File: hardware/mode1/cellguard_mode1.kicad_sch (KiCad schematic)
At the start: 19 parts, among them J1 Raspberry Pi 5 GPIO Header, J2 ZY12PDN PD Trigger (5V), J3 ATORCH BW150 부하 입력, K1 4CH Relay [SZH-RLBG-012], U1 INA226 [VLT-VCM029], U2 Battery Babysitter [PRT-13777], U3 MLX90614 [SEN0206], U4 ADS1115 [VLT-AD004], U5 DS18B20 방수형 [SEN050007], U6 OLED 0.96in SPI [CN0219]

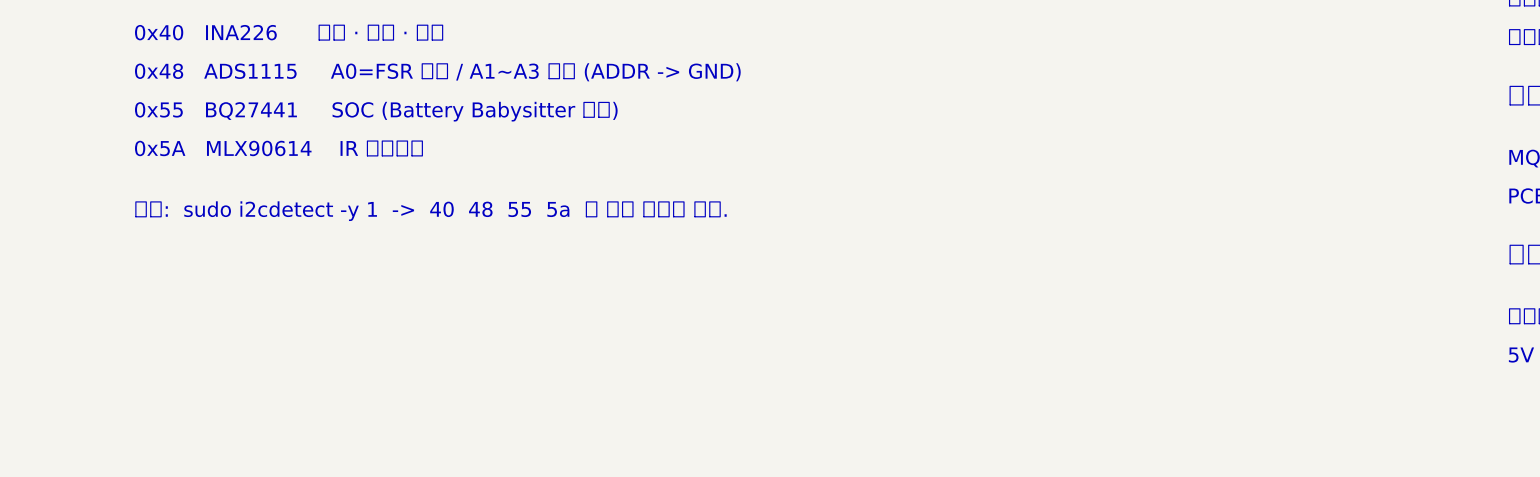
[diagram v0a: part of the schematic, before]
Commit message: fix(hw): MLX90614 갱신주기 정정(500ms -> 864.9ms)과 피크값 정책 확립
갱신주기 재확인 결과 이전에 적은 "약 500ms"가 틀렸다. Melexis 앱노트의
정착시간 공식 Tset = 9.719 + IIR x (FIR+5.26) + IIR x (FIR+12.542) 에
공장 기본값(IIR 50% -> IIRSetting 10, FIR 1024 -> FIRSetting 33.856)을
넣으면 864.859ms 로, 앱노트가 명시한 기본값과 정확히 일치한다. 즉
MLX90614는 DS18B20(750ms)보다도 느린, BQ27441 다음으로 느린 센서였다.

피크값 사용 요청에 대해 두 가지를 분리했다.

- 공간 피크(FOV 안 최고온점)는 불가능하다. MLX90614는 서모파일 소자
  1개짜리라 데이터시트가 "measured value is the average temperature of
  all objects in the Field Of View" 라고 명시한다. 설정이 아니라 물리다.
  대신 SEN0206(= MLX90614-DCC, FOV 35도)의 스팟 지름이 0.63 x 거리 이므로
  셀에서 2cm 이내에 부착하면 1.26cm 로 18650 지름 안에 들어가 배경이
  섞이지 않는다. 5cm 면 3.15cm 라 배경이 절반 넘게 섞인다.

- 시간축 피크(100ms 창의 최댓값)는 가능하되 EEPROM 재설정이 선행돼야
  한다. 공장 기본 IIR 50% 는 "최대 스텝 0.5" 라 입력이 튀어도 출력이
  절반까지만 따라간다 - 열폭주 초기 스파이크가 바로 그 신호인데 기본
  설정이 이를 깎아낸다. IIR=100(감쇠 없음) + FIR=111 로 바꾸면 95.2ms 가
  되어 100ms 프레임에 실측으로 들어온다. FIR=110 이면 62.5ms(창당 2샘플,
  노이즈 약 1.23배).

ConfigRegister1(EEPROM 0x05, SMBus 커맨드 0x25)의 비트 3은 건드리면
공장 캘리브레이션이 취소되므로 read-modify-write 를 강제했다.

Co-Authored-By: Claude Opus 5 <noreply@anthropic.com>
Claude-Session: https://claude.ai/code/session_01P42KJDHQDoWwm91ffeSx77
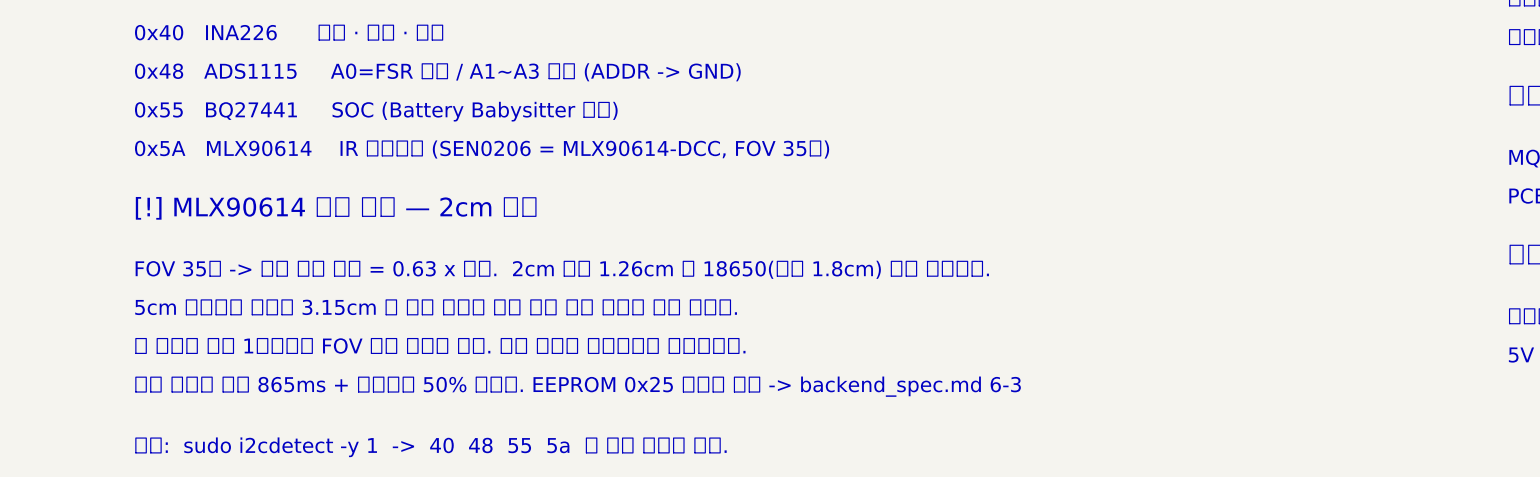
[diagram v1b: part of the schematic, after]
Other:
- note added: "0x5A MLX90614 IR 표면온도 (SEN0206 = MLX90614-DCC, FOV 35도)"
- note added: "5cm 떨어지면 스팟이 3.15cm 라 배경 온도가 절반 넘게 섞여 셀보다 낮게 읽힌다."
- note added: "FOV 35도 -> 측정 스팟 지름 = 0.63 x 거리. 2cm 에서 1.26cm 로 18650(지름 1.8cm) 안에 들어간다."
- note added: "[!] MLX90614 부착 거리 — 2cm 이내"
- note added: "이 센서는 소자 1개짜리라 FOV 안의 평균만 낸다. 공간 피크는 물리적으로 불가능하다."
- note added: "출고 상태는 갱신 865ms + 스파이크 50% 감쇠다. EEPROM 0x25 재설정 필수 -> backend_spec.md 6-3"
- note removed: "0x5A MLX90614 IR 표면온도"
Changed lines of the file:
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@@
 		(effects (font (face "Apple SD Gothic Neo") (size 2.0 2.0)) (justify left bottom))
 	)
-	(text "0x5A   MLX90614    IR 표면온도"
+	(text "0x5A   MLX90614    IR 표면온도 (SEN0206 = MLX90614-DCC, FOV 35도)"
 		(exclude_from_sim no)
 		(at 215.00 369.20 0)
 		(effects (font (face "Apple SD Gothic Neo") (size 2.0 2.0)) (justify left bottom))
 	)
+	(text "[!] MLX90614 부착 거리 — 2cm 이내"
+		(exclude_from_sim no)
+		(at 215.00 377.40 0)
+		(effects (font (face "Apple SD Gothic Neo") (size 2.5 2.5)) (justify left bottom))
+	)
+	(text "FOV 35도 -> 측정 스팟 지름 = 0.63 x 거리.  2cm 에서 1.26cm 로 18650(지름 1.8cm) 안에 들어간다."
+		(exclude_from_sim no)
+		(at 215.00 385.40 0)
+		(effects (font (face "Apple SD Gothic Neo") (size 2.0 2.0)) (justify left bottom))
+	)
+	(text "5cm 떨어지면 스팟이 3.15cm 라 배경 온도가 절반 넘게 섞여 셀보다 낮게 읽힌다."
+		(exclude_from_sim no)
+		(at 215.00 390.60 0)
+		(effects (font (face "Apple SD Gothic Neo") (size 2.0 2.0)) (justify left bottom))
+	)
+	(text "이 센서는 소자 1개짜리라 FOV 안의 평균만 낸다. 공간 피크는 물리적으로 불가능하다."
+		(exclude_from_sim no)
+		(at 215.00 395.80 0)
+		(effects (font (face "Apple SD Gothic Neo") (size 2.0 2.0)) (justify left bottom))
+	)
+	(text "출고 상태는 갱신 865ms + 스파이크 50% 감쇠다. EEPROM 0x25 재설정 필수 -> backend_spec.md 6-3"
+		(exclude_from_sim no)
+		(at 215.00 401.00 0)
+		(effects (font (face "Apple SD Gothic Neo") (size 2.0 2.0)) (justify left bottom))
+	)
 	(text "확인:  sudo i2cdetect -y 1  ->  40  48  55  5a  네 개가 보여야 한다."
 		(exclude_from_sim no)
-		(at 215.00 377.40 0)
+		(at 215.00 409.20 0)
 		(effects (font (face "Apple SD Gothic Neo") (size 2.0 2.0)) (justify left bottom))
 	)

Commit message: feat(hw): 온도를 다점 측정으로 확장해 공간 피크 구현
MLX90614 소자 1개는 데이터시트대로 FOV 안 모든 물체의 '평균'만 낸다.
열폭주는 국부에서 시작하므로 센서 1개로는 한 귀퉁이의 과열이 희석돼
사라진다. 억지로라도 공간 피크를 만들 방법을 찾다가 프로젝트 문서의
제약 하나가 사실이 아님을 확인했다.

MLX90614는 I2C 주소가 고정이 아니다. 데이터시트 EEPROM 맵에
"SMBus address (LSB only) | 0x0E | Write access: Yes" 로 명시돼 있고
Figure 36 이 "Use of multiple MLX90614 devices in SMBus network" 다.
한 버스에 127개까지 붙는다. 고정인 건 BQ27441(0x55) 뿐이므로
CLAUDE.md / PLAN.md / AGENTS.md 의 "둘 다 주소 고정" 서술을 정정했다.

그래서 예비품으로 잡아 뒀던 센서를 전부 투입해 다점화했다.

- DS18B20 x3 -> 셀 하단 / 중앙 / 단자쪽. 같은 GPIO4 버스에 병렬.
  1-Wire 는 고유 64비트 ROM 코드를 쓰므로 주소 설정이 필요 없고,
  Skip ROM + Convert T 로 동시 변환하면 개수가 늘어도 750ms 그대로다.
- MLX90614 x2 -> 셀 중앙(0x5A) / 단자쪽(0x5B). 양극 단자 부근이
  내부저항 + 접촉저항 때문에 가장 먼저 뜨거워지는 지점이다.
- temp_contact / temp_ir_surface 는 각 그룹의 최댓값. IR 은 시간축
  피크(창 안 최댓값) 위에 공간축 피크(두 존 중 큰 쪽)를 얹는다.
- temp_points 로 개별 지점값을 함께 발행한다(길이 고정 3/2, 위치 순서,
  결측은 null). 지점 간 온도차 자체가 국부 과열의 직접 증거다.
  기존 스칼라 필드는 그대로라 AI/대시보드 소비자는 고칠 게 없다.

시트가 A2 로는 주석을 못 담아 A1 으로 키우고 열 간격을 넓혔다.

검증: ERC 위반 0건. 네트리스트로 OW_DATA 5노드(U5/U7/U8 포함),
I2C_SDA/SCL 각 6노드(U9 포함), CELL_N 이 GND 와 분리된 것 재확인.

Co-Authored-By: Claude Opus 5 <noreply@anthropic.com>
Claude-Session: https://claude.ai/code/session_01P42KJDHQDoWwm91ffeSx77
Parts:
- added U7: DS18B20 #2 (셀 중앙), symbol cellguard:DS18B20
- added U8: DS18B20 #3 (셀 상단·단자쪽), symbol cellguard:DS18B20
- added U9: MLX90614 #2 (0x5B, 셀 단자쪽), symbol cellguard:MLX90614
- U3: value MLX90614 [SEN0206] -> MLX90614 #1 (0x5A, 셀 중앙)
- U5: value DS18B20 방수형 [SEN050007] -> DS18B20 #1 (셀 하단)
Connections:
- net +3V3: now also U7.1 (VDD), U8.1 (VDD), U9.1 (VCC)
- net GND: now also U7.3 (GND), U8.3 (GND), U9.2 (GND)
- net I2C_SCL: now also U9.4 (SCL)
- net I2C_SDA: now also U9.3 (SDA)
- net OW_DATA: now also U7.2 (DQ), U8.2 (DQ)
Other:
- note added: "0x5A MLX90614 #1 IR 표면온도 - 셀 중앙 (SEN0206 = MLX90614-DCC, FOV 35도)"
- note added: "0x5B MLX90614 #2 IR 표면온도 - 셀 단자쪽 (EEPROM 0x0E 로 주소 변경한 개체)"
- note added: "5V 3A+ 어댑터, 캡톤 테이프 · 서멀 패드 x3, 외장 케이스."
- note added: "DS18B20 3개는 같은 3선(GPIO4 + 3.3V + GND)에 병렬로 문다. 1-Wire는 고유 64비트 ROM 코드를"
- note added: "MLX90614 소자 1개는 FOV 안의 '평균'만 낸다. 그래서 2개를 다른 지점에 겨눠 공간 피크를 만든다."
- note added: "[!] 온도는 다점 측정 -> 최댓값을 쓴다"
- note added: "temp_ir_surface = max(#1, #2) temp_contact = max(DS18B20 #1, #2, #3)"
- note added: "물리핀 7 GPIO4 1-Wire (+ 4.7k 풀업 -> 3.3V) -> DS18B20 x3 (병렬)"
- note added: "쓰므로 주소 설정이 필요 없다. Skip ROM + Convert T 로 셋을 동시에 변환해 750ms 그대로다."
- note added: "예비품 없음: DS18B20 3개와 MLX90614 2개를 전부 투입했다. 고장 시 교체품이 없다."
- note removed: "0x5A MLX90614 IR 표면온도 (SEN0206 = MLX90614-DCC, FOV 35도)"
- note removed: "5V 3A+ 어댑터, 캡톤 테이프 · 서멀 패드, 외장 케이스."
- note removed: "물리핀 7 GPIO4 1-Wire (+ 4.7k 풀업 -> 3.3V) -> DS18B20"
- note removed: "이 센서는 소자 1개짜리라 FOV 안의 평균만 낸다. 공간 피크는 물리적으로 불가능하다."
- moved on the sheet: J1, J2, J3, K1, R2, R3, R4, R5, R6, U2, U3, U4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

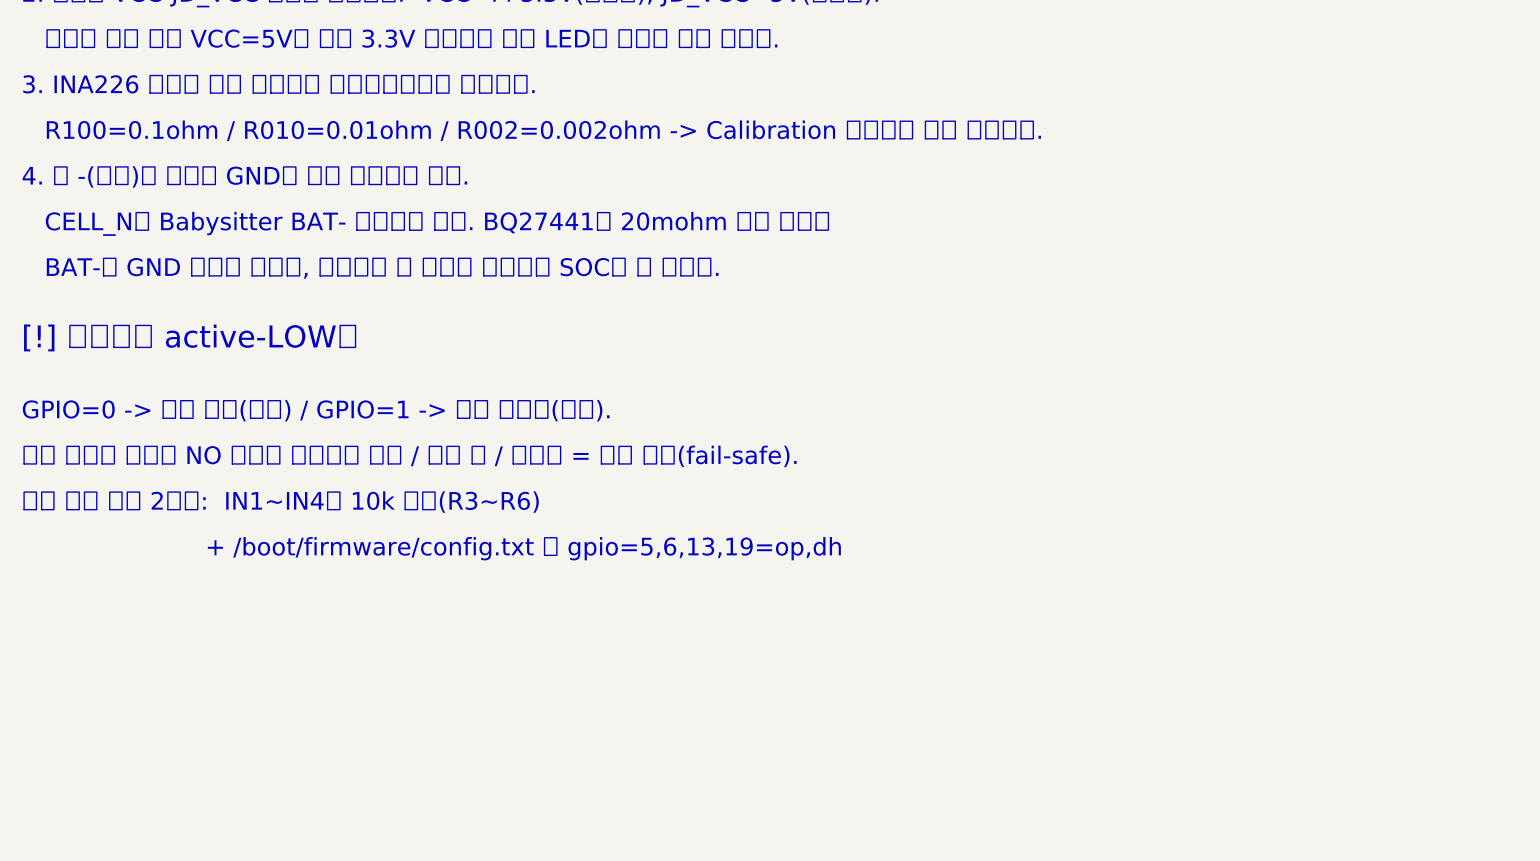
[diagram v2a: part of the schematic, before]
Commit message: fix(hw): 백엔드 스펙 검증 — 치명적 사실오류 3건 정정, §1 재작성
Sonnet 5 서브에이전트 2대로 데이터시트 대조 검증과 문서 정합성 감사를
돌리고, 치명적 지적은 원문으로 직접 재확인한 뒤 반영했다.

## 치명적 사실오류 (구현했다면 조용히 틀렸을 것들)

1. BQ27441 Flags(0x06) 비트 3개가 틀렸다. TRM Table 4-4 가 High/Low
   바이트를 각각 bit7..bit0 으로 표기하는데 이를 절대 비트로 잘못
   환산했다. ITPOR 은 bit 8 이 아니라 bit 5 이고, bit 8 은 CHG(충전
   허용)다. 옛 표대로 구현하면 충전할 때마다 "게이지 리셋됨"으로
   오탐하고 정작 진짜 리셋(ITPOR)은 영영 못 잡는다. OT 는 bit 15,
   FC 는 bit 9 로 서로 뒤바뀌어 있었다.

2. BQ27441 AveragePower 주소가 0x16 이 아니라 0x18 이다. 0x16/0x17 은
   표준 커맨드에 존재하지 않는 주소다. (TRM Table 4-1)

3. INA226 "최대 측정 전류 20A/8A/0.8A" 가 틀렸다. 상한을 정하는 건
   션트가 아니라 16비트 Current 레지스터다. Current_LSB=0.0001A 면
   션트값과 무관하게 32767 x 0.0001 = 3.28A 에서 넘치고, 넘치면 부호가
   뒤집혀 방전이 충전으로 보인다. 실제 상한은 3.28/3.28/0.82A.
   TI 가 이 실패모드용으로 Mask/Enable(0x06) bit 2 에 OVF 플래그를
   두었으므로 매 프레임 확인하도록 오류 처리에 추가했다.

## §1 재작성

MLX90614 가 500ms 이고 센서가 각 1개이던 시절 문장이 남아 있었다.
- "새 값이 나오는 센서는 INA226 하나뿐" -> 표에 ADS1115 가 7.8ms 로
  적혀 있어 자기모순이었다. INA226 + ADS1115 로 정정.
- "온도는 7~8개가 복사본" -> 두 온도 필드의 주기가 이제 완전히 다르다.
  IR 은 재설정 후 매 프레임 실측, 접촉은 750ms 고정으로 분리 서술.
- "가장 느린 센서(750ms)" -> BQ27441 1000ms, bulk read 미지원 시
  DS18B20 2250ms 로 정정.
- 신선도 예시 JSON 에 temp_points 추가. MLX 2개는 순차 읽기라 지점
  간 age 가 어긋날 수 있음을 명시.
- 9비트 옵션이 3개 동시 변환에도 그대로 적용됨을 명시.

## 그 밖

- MLX90614 노이즈 관계 인용의 출처를 앱노트 -> 데이터시트로 정정.
  원문은 정착시간이 아니라 탭 수 기준이라 1024->512 는 1.23배가 아니라
  약 1.41배(√2)다.
- Pi 5 에서 config.txt 의 gpio= 지시문이 동작하는지는 확인이 필요하다.
  공식 문서는 여전히 문서화하고 Pi 5 제외 문구도 없으므로 "동작 안 함"
  으로 단정하지 않고, 3겹 방어 중 하드웨어 풀업만이 소프트웨어에
  의존하지 않는 층임을 명시하고 확인법(pinctrl get)을 넣었다.
- §6 헤더를 MLX90614 x2 (0x5A/0x5B) 로 복수화.
- PLAN.md 줄번호 인용 8건이 전부 깨져 있어 절 이름 인용으로 바꿨다.
  줄번호는 문서가 편집될 때마다 다시 깨진다.
- §14 "실물로 확인해야 하는 것" 신설 (H1~H7).

검증: ERC 위반 0건. 문서 내 §참조 전수 검사 결과 깨진 참조 0건.

Co-Authored-By: Claude Opus 5 <noreply@anthropic.com>
Claude-Session: https://claude.ai/code/session_01P42KJDHQDoWwm91ffeSx77
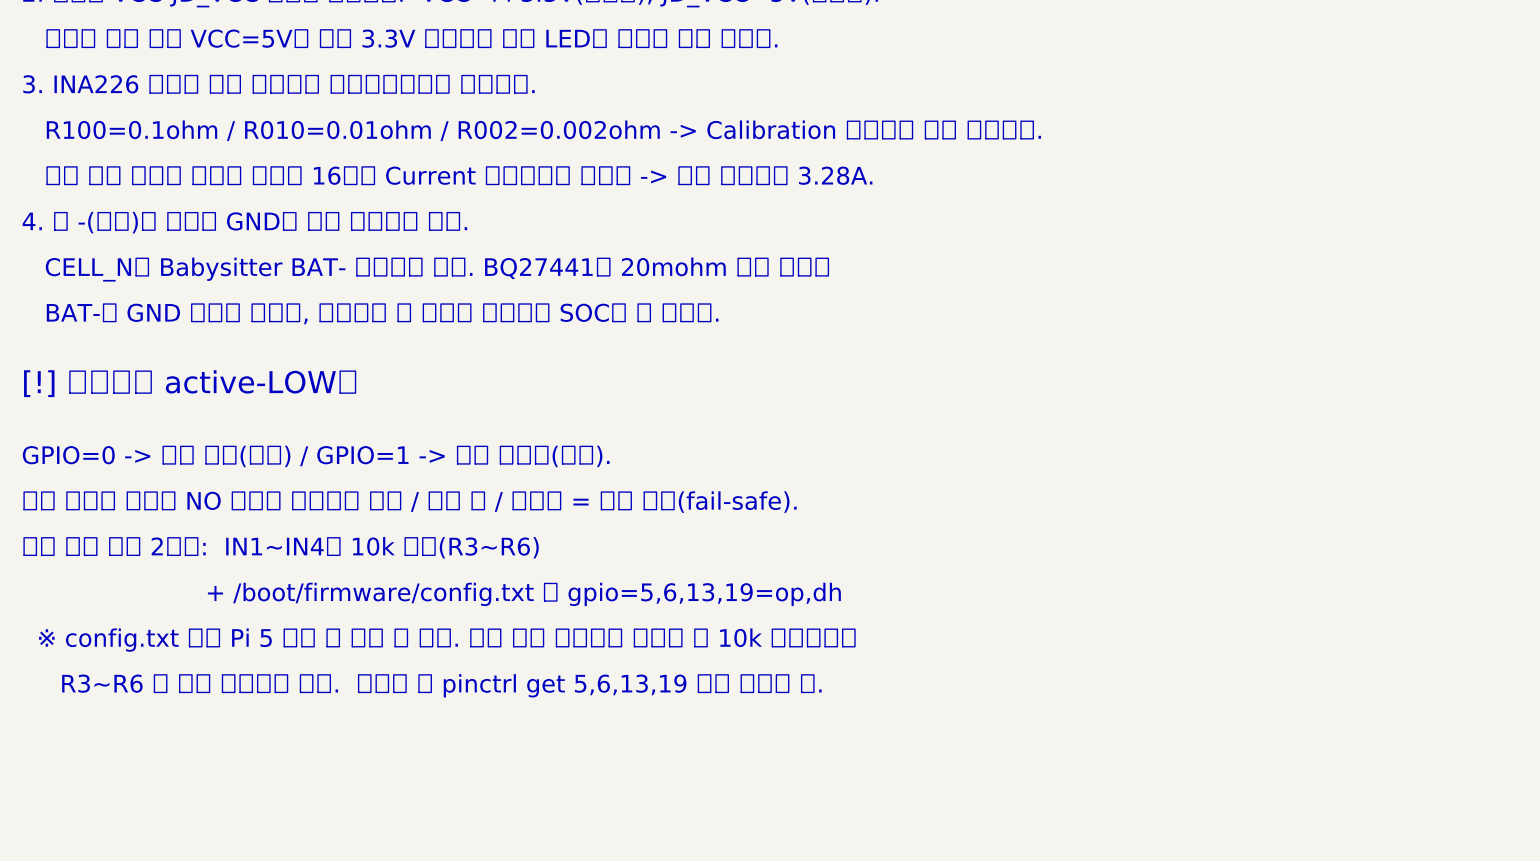
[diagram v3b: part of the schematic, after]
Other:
- note added: "R3~R6 을 절대 생략하지 마라. 재부팅 후 pinctrl get 5,6,13,19 으로 확인할 것."
- note added: "※ config.txt 쪽은 Pi 5 에서 안 먹을 수 있다. 전원 인가 순간부터 확실한 건 10k 풀업뿐이니"
- note added: "전류 측정 상한은 션트가 아니라 16비트 Current 레지스터가 정한다 -> 기본 설정에서 3.28A."
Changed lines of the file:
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@@
+		(effects (font (face "Apple SD Gothic Neo") (size 2.0 2.0)) (justify left bottom))
+	)
+	(text "   전류 측정 상한은 션트가 아니라 16비트 Current 레지스터가 정한다 -> 기본 설정에서 3.28A."
+		(exclude_from_sim no)
+		(at 20.00 371.80 0)
 		(effects (font (face "Apple SD Gothic Neo") (size 2.0 2.0)) (justify left bottom))
 	)
 	(text "4. 셀 -(음극)를 시스템 GND에 직접 연결하지 마라."
 		(exclude_from_sim no)
-		(at 20.00 371.80 0)
+		(at 20.00 377.00 0)
 		(effects (font (face "Apple SD Gothic Neo") (size 2.0 2.0)) (justify left bottom))
 	)
 	(text "   CELL_N은 Babysitter BAT- 하나에만 간다. BQ27441의 20mohm 센스 저항이"
 		(exclude_from_sim no)
-		(at 20.00 377.00 0)
+		(at 20.00 382.20 0)
 		(effects (font (face "Apple SD Gothic Neo") (size 2.0 2.0)) (justify left bottom))
 	)
 	(text "   BAT-와 GND 사이에 있어서, 직결하면 이 저항이 단락되고 SOC가 안 나온다."
 		(exclude_from_sim no)
-		(at 20.00 382.20 0)
+		(at 20.00 387.40 0)
 		(effects (font (face "Apple SD Gothic Neo") (size 2.0 2.0)) (justify left bottom))
 	)
 	(text "[!] 릴레이는 active-LOW다"
 		(exclude_from_sim no)
-		(at 20.00 390.40 0)
+		(at 20.00 395.60 0)
 		(effects (font (face "Apple SD Gothic Neo") (size 2.5 2.5)) (justify left bottom))
 	)
 	(text "GPIO=0 -> 접점 붙음(도통) / GPIO=1 -> 접점 떨어짐(차단)."
 		(exclude_from_sim no)
-		(at 20.00 398.40 0)
+		(at 20.00 403.60 0)
 		(effects (font (face "Apple SD Gothic Neo") (size 2.0 2.0)) (justify left bottom))
 	)
 	(text "모든 배터리 경로가 NO 접점을 지나므로 정전 / 부팅 중 / 크래시 = 자동 차단(fail-safe)."
 		(exclude_from_sim no)
-		(at 20.00 403.60 0)
+		(at 20.00 408.80 0)
 		(effects (font (face "Apple SD Gothic Neo") (size 2.0 2.0)) (justify left bottom))
 	)
 	(text "부팅 초기 보호 2중화:  IN1~IN4에 10k 풀업(R3~R6)"
 		(exclude_from_sim no)
-		(at 20.00 408.80 0)
+		(at 20.00 414.00 0)
 		(effects (font (face "Apple SD Gothic Neo") (size 2.0 2.0)) (justify left bottom))
 	)
 	(text "                        + /boot/firmware/config.txt 에 gpio=5,6,13,19=op,dh"
 		(exclude_from_sim no)
-		(at 20.00 414.00 0)
+		(at 20.00 419.20 0)
 		(effects (font (face "Apple SD Gothic Neo") (size 2.0 2.0)) (justify left bottom))
 	)
+	(text "  ※ config.txt 쪽은 Pi 5 에서 안 먹을 수 있다. 전원 인가 순간부터 확실한 건 10k 풀업뿐이니"
+		(exclude_from_sim no)
+		(at 20.00 424.40 0)
+		(effects (font (face "Apple SD Gothic Neo") (size 2.0 2.0)) (justify left bottom))
+	)
+	(text "     R3~R6 을 절대 생략하지 마라.  재부팅 후 pinctrl get 5,6,13,19 으로 확인할 것."
+		(exclude_from_sim no)
+		(at 20.00 429.60 0)
+		(effects (font (face "Apple SD Gothic Neo") (size 2.0 2.0)) (justify left bottom))
+	)
